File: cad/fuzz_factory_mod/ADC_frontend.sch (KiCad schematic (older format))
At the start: 11 parts

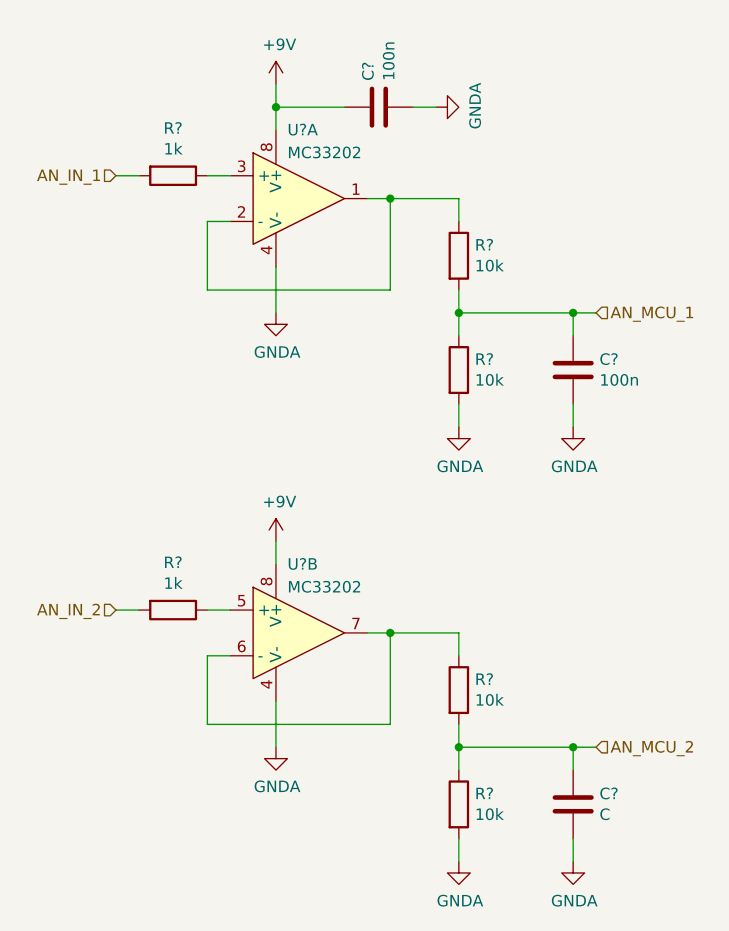
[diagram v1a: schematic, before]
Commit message: Continued schematic.
Modified fuuz_factory circuit : use of matched transistor pairs.
Added USB interface, through FT230X and direct to MCU.
Associated footprints, except for XTAL and trimmers.
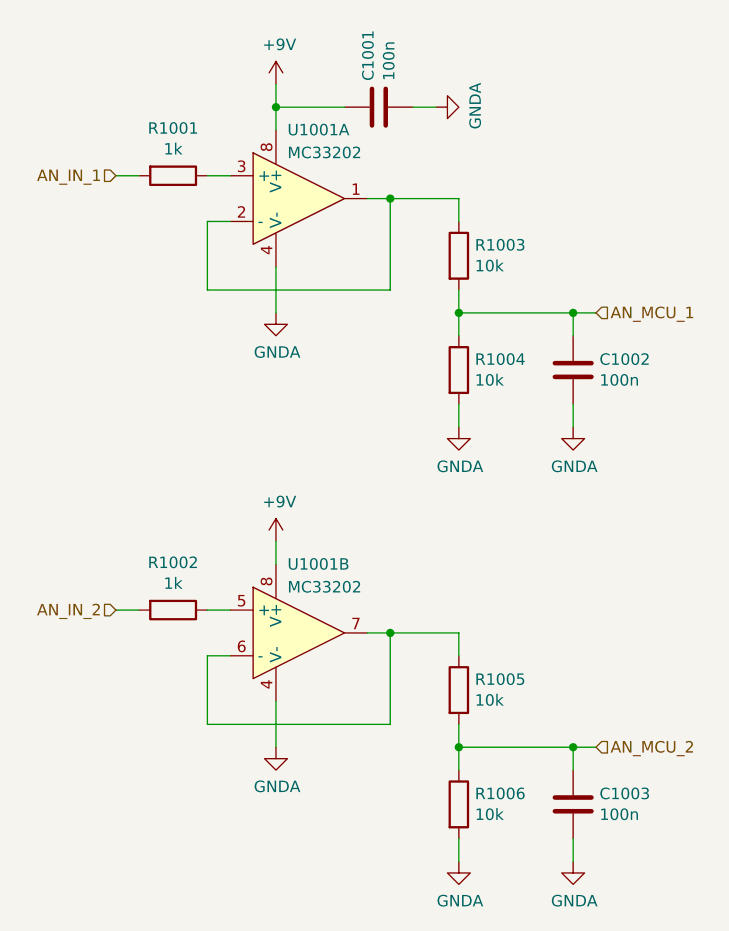
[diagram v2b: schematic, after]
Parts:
- C1001, C1002: renamed from C?; footprint (none) -> Capacitors_SMD:C_0603
- C1003: renamed from C?; value C -> 100n; footprint (none) -> Capacitors_SMD:C_0603
- R1001, R1002, R1003, R1004, R1005, R1006: renamed from R?; footprint (none) -> Resistors_SMD:R_0603
- U1001: renamed from U?; footprint (none) -> Housings_SOIC:SOIC-8_3.9x4.9mm_Pitch1.27mm
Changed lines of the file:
@@
 $Descr A4 11693 8268
 encoding utf-8
-Sheet 8 19
+Sheet 10 22
 Title ""
 Date ""
@@
 $EndDescr
 $Comp
-L power:+9V #PWR?
+L power:+9V #PWR01001
 U 1 1 5E671148
 P 2200 1600
-F 0 "#PWR?" H 2200 1450 50  0001 C CNN
+F 0 "#PWR01001" H 2200 1450 50  0001 C CNN
 F 1 "+9V" H 2215 1773 50  0000 C CNN
 F 2 "" H 2200 1600 50  0001 C CNN
@@
 $EndComp
 $Comp
-L power:GNDA #PWR?
+L power:GNDA #PWR01002
 U 1 1 5E672355
 P 2200 2600
-F 0 "#PWR?" H 2200 2350 50  0001 C CNN
+F 0 "#PWR01002" H 2200 2350 50  0001 C CNN
 F 1 "GNDA" H 2205 2427 50  0000 C CNN
 F 2 "" H 2200 2600 50  0001 C CNN
@@
 	2700 2100 2600 2100
 $Comp
-L flax_lib:MC33202 U?
+L flax_lib:MC33202 U1001
 U 1 1 5E66FC5B
 P 2300 2100
-F 0 "U?" H 2250 2400 50  0000 L CNN
+F 0 "U1001" H 2250 2400 50  0000 L CNN
 F 1 "MC33202" H 2250 2300 50  0000 L CNN
-F 2 "" H 2300 2100 50  0000 C CNN
+F 2 "Housings_SOIC:SOIC-8_3.9x4.9mm_Pitch1.27mm" H 2300 2100 50  0001 C CNN
 F 3 "" H 2250 1900 50  0000 L CNN
 	1    2300 2100
@@
 $EndComp
 $Comp
-L Device:R R?
+L Device:R R1003
 U 1 1 5E673C44
 P 3000 2350
-F 0 "R?" H 3070 2396 50  0000 L CNN
+F 0 "R1003" H 3070 2396 50  0000 L CNN
 F 1 "10k" H 3070 2305 50  0000 L CNN
-F 2 "" V 2930 2350 50  0001 C CNN
+F 2 "Resistors_SMD:R_0603" V 2930 2350 50  0001 C CNN
 F 3 "~" H 3000 2350 50  0001 C CNN
 	1    3000 2350
@@
 $EndComp
 $Comp
-L Device:R R?
+L Device:R R1004
 U 1 1 5E6750F5
 P 3000 2850
-F 0 "R?" H 3070 2896 50  0000 L CNN
+F 0 "R1004" H 3070 2896 50  0000 L CNN
 F 1 "10k" H 3070 2805 50  0000 L CNN
-F 2 "" V 2930 2850 50  0001 C CNN
+F 2 "Resistors_SMD:R_0603" V 2930 2850 50  0001 C CNN
 F 3 "~" H 3000 2850 50  0001 C CNN
 	1    3000 2850
@@
 $EndComp
 $Comp
-L power:GNDA #PWR?
+L power:GNDA #PWR01006
 U 1 1 5E6758D7
 P 3000 3100
-F 0 "#PWR?" H 3000 2850 50  0001 C CNN
+F 0 "#PWR01006" H 3000 2850 50  0001 C CNN
 F 1 "GNDA" H 3005 2927 50  0000 C CNN
 F 2 "" H 3000 3100 50  0001 C CNN
@@
 Connection ~ 2700 2100
 $Comp
-L Device:C C?
+L Device:C C1002
 U 1 1 5E676167
 P 3500 2850
-F 0 "C?" H 3615 2896 50  0000 L CNN
+F 0 "C1002" H 3615 2896 50  0000 L CNN
 F 1 "100n" H 3615 2805 50  0000 L CNN
-F 2 "" H 3538 2700 50  0001 C CNN
+F 2 "Capacitors_SMD:C_0603" H 3538 2700 50  0001 C CNN
 F 3 "~" H 3500 2850 50  0001 C CNN
 	1    3500 2850
@@
 	3000 2600 3000 2500
 $Comp
-L power:GNDA #PWR?
+L power:GNDA #PWR01008
 U 1 1 5E6770AE
 P 3500 3100
-F 0 "#PWR?" H 3500 2850 50  0001 C CNN
+F 0 "#PWR01008" H 3500 2850 50  0001 C CNN
 F 1 "GNDA" H 3505 2927 50  0000 C CNN
 F 2 "" H 3500 3100 50  0001 C CNN
@@
 	3500 3000 3500 3100
 $Comp
-L Device:R R?
+L Device:R R1001
 U 1 1 5E6776A2
 P 1750 2000
-F 0 "R?" V 1543 2000 50  0000 C CNN
+F 0 "R1001" V 1543 2000 50  0000 C CNN
 F 1 "1k" V 1634 2000 50  0000 C CNN
-F 2 "" V 1680 2000 50  0001 C CNN
+F 2 "Resistors_SMD:R_0603" V 1680 2000 50  0001 C CNN
 F 3 "~" H 1750 2000 50  0001 C CNN
 	1    1750 2000
@@
 Connection ~ 3500 2600
 $Comp
-L power:+9V #PWR?
+L power:+9V #PWR01003
 U 1 1 5E678DD1
 P 2200 3600
-F 0 "#PWR?" H 2200 3450 50  0001 C CNN
+F 0 "#PWR01003" H 2200 3450 50  0001 C CNN
 F 1 "+9V" H 2215 3773 50  0000 C CNN
 F 2 "" H 2200 3600 50  0001 C CNN
@@
 	2200 3600 2200 3700
 $Comp
-L power:GNDA #PWR?
+L power:GNDA #PWR01004
 U 1 1 5E678DDC
 P 2200 4500
-F 0 "#PWR?" H 2200 4250 50  0001 C CNN
+F 0 "#PWR01004" H 2200 4250 50  0001 C CNN
 F 1 "GNDA" H 2205 4327 50  0000 C CNN
 F 2 "" H 2200 4500 50  0001 C CNN
@@
 	2700 4000 2600 4000
 $Comp
-L flax_lib:MC33202 U?
+L flax_lib:MC33202 U1001
 U 2 1 5E678DEC
 P 2300 4000
-F 0 "U?" H 2250 4300 50  0000 L CNN
+F 0 "U1001" H 2250 4300 50  0000 L CNN
 F 1 "MC33202" H 2250 4200 50  0000 L CNN
-F 2 "" H 2300 4000 50  0000 C CNN
+F 2 "Housings_SOIC:SOIC-8_3.9x4.9mm_Pitch1.27mm" H 2300 4000 50  0001 C CNN
 F 3 "" H 2250 3800 50  0000 L CNN
 	2    2300 4000
@@
 $EndComp
 $Comp
-L Device:R R?
+L Device:R R1005
 U 1 1 5E678DF6
 P 3000 4250
-F 0 "R?" H 3070 4296 50  0000 L CNN
+F 0 "R1005" H 3070 4296 50  0000 L CNN
 F 1 "10k" H 3070 4205 50  0000 L CNN
-F 2 "" V 2930 4250 50  0001 C CNN
+F 2 "Resistors_SMD:R_0603" V 2930 4250 50  0001 C CNN
 F 3 "~" H 3000 4250 50  0001 C CNN
 	1    3000 4250
@@
 $EndComp
 $Comp
-L Device:R R?
+L Device:R R1006
 U 1 1 5E678E00
 P 3000 4750
-F 0 "R?" H 3070 4796 50  0000 L CNN
+F 0 "R1006" H 3070 4796 50  0000 L CNN
 F 1 "10k" H 3070 4705 50  0000 L CNN
-F 2 "" V 2930 4750 50  0001 C CNN
+F 2 "Resistors_SMD:R_0603" V 2930 4750 50  0001 C CNN
 F 3 "~" H 3000 4750 50  0001 C CNN
 	1    3000 4750
@@
 $EndComp
 $Comp
-L power:GNDA #PWR?
+L power:GNDA #PWR01007
 U 1 1 5E678E0A
 P 3000 5000
-F 0 "#PWR?" H 3000 4750 50  0001 C CNN
+F 0 "#PWR01007" H 3000 4750 50  0001 C CNN
 F 1 "GNDA" H 3005 4827 50  0000 C CNN
 F 2 "" H 3000 5000 50  0001 C CNN
@@
 Connection ~ 2700 4000
 $Comp
-L Device:C C?
+L Device:C C1003
 U 1 1 5E678E19
 P 3500 4750
-F 0 "C?" H 3615 4796 50  0000 L CNN
-F 1 "C" H 3615 4705 50  0000 L CNN
-F 2 "" H 3538 4600 50  0001 C CNN
+F 0 "C1003" H 3615 4796 50  0000 L CNN
+F 1 "100n" H 3615 4705 50  0000 L CNN
+F 2 "Capacitors_SMD:C_0603" H 3538 4600 50  0001 C CNN
 F 3 "~" H 3500 4750 50  0001 C CNN
 	1    3500 4750
@@
 	3000 4500 3000 4400
 $Comp
-L power:GNDA #PWR?
+L power:GNDA #PWR01009
 U 1 1 5E678E27
 P 3500 5000
-F 0 "#PWR?" H 3500 4750 50  0001 C CNN
+F 0 "#PWR01009" H 3500 4750 50  0001 C CNN
 F 1 "GNDA" H 3505 4827 50  0000 C CNN
 F 2 "" H 3500 5000 50  0001 C CNN
@@
 	3500 4900 3500 5000
 $Comp
-L Device:R R?
+L Device:R R1002
 U 1 1 5E678E32
 P 1750 3900
-F 0 "R?" V 1543 3900 50  0000 C CNN
+F 0 "R1002" V 1543 3900 50  0000 C CNN
 F 1 "1k" V 1634 3900 50  0000 C CNN
-F 2 "" V 1680 3900 50  0001 C CNN
+F 2 "Resistors_SMD:R_0603" V 1680 3900 50  0001 C CNN
 F 3 "~" H 1750 3900 50  0001 C CNN
 	1    1750 3900
@@
 Connection ~ 3500 4500
 $Comp
-L Device:C C?
+L Device:C C1001
 U 1 1 5E687CFA
 P 2650 1700
-F 0 "C?" H 2765 1746 50  0000 L CNN
+F 0 "C1001" H 2765 1746 50  0000 L CNN
 F 1 "100n" H 2765 1655 50  0000 L CNN
-F 2 "" H 2688 1550 50  0001 C CNN
+F 2 "Capacitors_SMD:C_0603" H 2688 1550 50  0001 C CNN
 F 3 "~" H 2650 1700 50  0001 C CNN
 	1    2650 1700
@@
 $EndComp
 $Comp
-L power:GNDA #PWR?
+L power:GNDA #PWR01005
 U 1 1 5E687D04
 P 2900 1700
-F 0 "#PWR?" H 2900 1450 50  0001 C CNN
+F 0 "#PWR01005" H 2900 1450 50  0001 C CNN
 F 1 "GNDA" H 2905 1527 50  0000 C CNN
 F 2 "" H 2900 1700 50  0001 C CNN

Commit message: Commit pre- board separation.
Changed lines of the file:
@@
 AR Path="/5DE4AD88/5E6E7BE0/5EEB4E87/5E671148" Ref="#PWR0119"  Part="1"
 AR Path="/5DE4AD88/5EB9A4D1/5ED2AE35/5E671148" Ref="#PWR02401"  Part="1"
-F 0 "#PWR0119" H 2200 1450 50  0001 C CNN
+F 0 "#PWR02401" H 2200 1450 50  0001 C CNN
 F 1 "+9V" H 2215 1773 50  0000 C CNN
 F 2 "" H 2200 1600 50  0001 C CNN
@@
 AR Path="/5DE4AD88/5E6E7BE0/5EEB4E87/5E672355" Ref="#PWR0120"  Part="1"
 AR Path="/5DE4AD88/5EB9A4D1/5ED2AE35/5E672355" Ref="#PWR02402"  Part="1"
-F 0 "#PWR0120" H 2200 2350 50  0001 C CNN
+F 0 "#PWR02402" H 2200 2350 50  0001 C CNN
 F 1 "GNDA" H 2205 2427 50  0000 C CNN
 F 2 "" H 2200 2600 50  0001 C CNN
@@
 AR Path="/5DE4AD88/5E6E7BE0/5EEB4E87/5E66FC5B" Ref="U1001"  Part="1"
 AR Path="/5DE4AD88/5EB9A4D1/5ED2AE35/5E66FC5B" Ref="U2401"  Part="1"
-F 0 "U1001" H 2250 2400 50  0000 L CNN
+F 0 "U2401" H 2250 2400 50  0000 L CNN
 F 1 "MC33202" H 2250 2300 50  0000 L CNN
 F 2 "Housings_SOIC:SOIC-8_3.9x4.9mm_Pitch1.27mm" H 2300 2100 50  0001 C CNN
@@
 AR Path="/5DE4AD88/5E6E7BE0/5EEB4E87/5E673C44" Ref="R1003"  Part="1"
 AR Path="/5DE4AD88/5EB9A4D1/5ED2AE35/5E673C44" Ref="R2403"  Part="1"
-F 0 "R1003" H 3070 2396 50  0000 L CNN
+F 0 "R2403" H 3070 2396 50  0000 L CNN
 F 1 "10k" H 3070 2305 50  0000 L CNN
 F 2 "Resistors_SMD:R_0603" V 2930 2350 50  0001 C CNN
@@
 AR Path="/5DE4AD88/5E6E7BE0/5EEB4E87/5E6750F5" Ref="R1004"  Part="1"
 AR Path="/5DE4AD88/5EB9A4D1/5ED2AE35/5E6750F5" Ref="R2404"  Part="1"
-F 0 "R1004" H 3070 2896 50  0000 L CNN
+F 0 "R2404" H 3070 2896 50  0000 L CNN
 F 1 "10k" H 3070 2805 50  0000 L CNN
 F 2 "Resistors_SMD:R_0603" V 2930 2850 50  0001 C CNN
@@
 AR Path="/5DE4AD88/5E6E7BE0/5EEB4E87/5E6758D7" Ref="#PWR0121"  Part="1"
 AR Path="/5DE4AD88/5EB9A4D1/5ED2AE35/5E6758D7" Ref="#PWR02406"  Part="1"
-F 0 "#PWR0121" H 3000 2850 50  0001 C CNN
+F 0 "#PWR02406" H 3000 2850 50  0001 C CNN
 F 1 "GNDA" H 3005 2927 50  0000 C CNN
 F 2 "" H 3000 3100 50  0001 C CNN
@@
 AR Path="/5DE4AD88/5E6E7BE0/5EEB4E87/5E676167" Ref="C1002"  Part="1"
 AR Path="/5DE4AD88/5EB9A4D1/5ED2AE35/5E676167" Ref="C2402"  Part="1"
-F 0 "C1002" H 3615 2896 50  0000 L CNN
+F 0 "C2402" H 3615 2896 50  0000 L CNN
 F 1 "100n" H 3615 2805 50  0000 L CNN
 F 2 "Capacitors_SMD:C_0603" H 3538 2700 50  0001 C CNN
@@
 AR Path="/5DE4AD88/5E6E7BE0/5EEB4E87/5E6770AE" Ref="#PWR0122"  Part="1"
 AR Path="/5DE4AD88/5EB9A4D1/5ED2AE35/5E6770AE" Ref="#PWR02408"  Part="1"
-F 0 "#PWR0122" H 3500 2850 50  0001 C CNN
+F 0 "#PWR02408" H 3500 2850 50  0001 C CNN
 F 1 "GNDA" H 3505 2927 50  0000 C CNN
 F 2 "" H 3500 3100 50  0001 C CNN
@@
 AR Path="/5DE4AD88/5E6E7BE0/5EEB4E87/5E6776A2" Ref="R1001"  Part="1"
 AR Path="/5DE4AD88/5EB9A4D1/5ED2AE35/5E6776A2" Ref="R2401"  Part="1"
-F 0 "R1001" V 1543 2000 50  0000 C CNN
+F 0 "R2401" V 1543 2000 50  0000 C CNN
 F 1 "1k" V 1634 2000 50  0000 C CNN
 F 2 "Resistors_SMD:R_0603" V 1680 2000 50  0001 C CNN
@@
 AR Path="/5DE4AD88/5E6E7BE0/5EEB4E87/5E678DD1" Ref="#PWR0123"  Part="1"
 AR Path="/5DE4AD88/5EB9A4D1/5ED2AE35/5E678DD1" Ref="#PWR02403"  Part="1"
-F 0 "#PWR0123" H 2200 3450 50  0001 C CNN
+F 0 "#PWR02403" H 2200 3450 50  0001 C CNN
 F 1 "+9V" H 2215 3773 50  0000 C CNN
 F 2 "" H 2200 3600 50  0001 C CNN
@@
 AR Path="/5DE4AD88/5E6E7BE0/5EEB4E87/5E678DDC" Ref="#PWR0124"  Part="1"
 AR Path="/5DE4AD88/5EB9A4D1/5ED2AE35/5E678DDC" Ref="#PWR02404"  Part="1"
-F 0 "#PWR0124" H 2200 4250 50  0001 C CNN
+F 0 "#PWR02404" H 2200 4250 50  0001 C CNN
 F 1 "GNDA" H 2205 4327 50  0000 C CNN
 F 2 "" H 2200 4500 50  0001 C CNN
@@
 AR Path="/5DE4AD88/5E6E7BE0/5EEB4E87/5E678DEC" Ref="U1001"  Part="2"
 AR Path="/5DE4AD88/5EB9A4D1/5ED2AE35/5E678DEC" Ref="U2401"  Part="2"
-F 0 "U1001" H 2250 4300 50  0000 L CNN
+F 0 "U2401" H 2250 4300 50  0000 L CNN
 F 1 "MC33202" H 2250 4200 50  0000 L CNN
 F 2 "Housings_SOIC:SOIC-8_3.9x4.9mm_Pitch1.27mm" H 2300 4000 50  0001 C CNN
@@
 AR Path="/5DE4AD88/5E6E7BE0/5EEB4E87/5E678DF6" Ref="R1005"  Part="1"
 AR Path="/5DE4AD88/5EB9A4D1/5ED2AE35/5E678DF6" Ref="R2405"  Part="1"
-F 0 "R1005" H 3070 4296 50  0000 L CNN
+F 0 "R2405" H 3070 4296 50  0000 L CNN
 F 1 "10k" H 3070 4205 50  0000 L CNN
 F 2 "Resistors_SMD:R_0603" V 2930 4250 50  0001 C CNN
@@
 AR Path="/5DE4AD88/5E6E7BE0/5EEB4E87/5E678E00" Ref="R1006"  Part="1"
 AR Path="/5DE4AD88/5EB9A4D1/5ED2AE35/5E678E00" Ref="R2406"  Part="1"
-F 0 "R1006" H 3070 4796 50  0000 L CNN
+F 0 "R2406" H 3070 4796 50  0000 L CNN
 F 1 "10k" H 3070 4705 50  0000 L CNN
 F 2 "Resistors_SMD:R_0603" V 2930 4750 50  0001 C CNN
@@
 AR Path="/5DE4AD88/5E6E7BE0/5EEB4E87/5E678E0A" Ref="#PWR0125"  Part="1"
 AR Path="/5DE4AD88/5EB9A4D1/5ED2AE35/5E678E0A" Ref="#PWR02407"  Part="1"
-F 0 "#PWR0125" H 3000 4750 50  0001 C CNN
+F 0 "#PWR02407" H 3000 4750 50  0001 C CNN
 F 1 "GNDA" H 3005 4827 50  0000 C CNN
 F 2 "" H 3000 5000 50  0001 C CNN
@@
 AR Path="/5DE4AD88/5E6E7BE0/5EEB4E87/5E678E19" Ref="C1003"  Part="1"
 AR Path="/5DE4AD88/5EB9A4D1/5ED2AE35/5E678E19" Ref="C2403"  Part="1"
-F 0 "C1003" H 3615 4796 50  0000 L CNN
+F 0 "C2403" H 3615 4796 50  0000 L CNN
 F 1 "100n" H 3615 4705 50  0000 L CNN
 F 2 "Capacitors_SMD:C_0603" H 3538 4600 50  0001 C CNN
@@
 AR Path="/5DE4AD88/5E6E7BE0/5EEB4E87/5E678E27" Ref="#PWR0126"  Part="1"
 AR Path="/5DE4AD88/5EB9A4D1/5ED2AE35/5E678E27" Ref="#PWR02409"  Part="1"
-F 0 "#PWR0126" H 3500 4750 50  0001 C CNN
+F 0 "#PWR02409" H 3500 4750 50  0001 C CNN
 F 1 "GNDA" H 3505 4827 50  0000 C CNN
 F 2 "" H 3500 5000 50  0001 C CNN
@@
 AR Path="/5DE4AD88/5E6E7BE0/5EEB4E87/5E678E32" Ref="R1002"  Part="1"
 AR Path="/5DE4AD88/5EB9A4D1/5ED2AE35/5E678E32" Ref="R2402"  Part="1"
-F 0 "R1002" V 1543 3900 50  0000 C CNN
+F 0 "R2402" V 1543 3900 50  0000 C CNN
 F 1 "1k" V 1634 3900 50  0000 C CNN
 F 2 "Resistors_SMD:R_0603" V 1680 3900 50  0001 C CNN
@@
 AR Path="/5DE4AD88/5E6E7BE0/5EEB4E87/5E687CFA" Ref="C1001"  Part="1"
 AR Path="/5DE4AD88/5EB9A4D1/5ED2AE35/5E687CFA" Ref="C2401"  Part="1"
-F 0 "C1001" H 2765 1746 50  0000 L CNN
+F 0 "C2401" H 2765 1746 50  0000 L CNN
 F 1 "100n" H 2765 1655 50  0000 L CNN
 F 2 "Capacitors_SMD:C_0603" H 2688 1550 50  0001 C CNN
@@
 AR Path="/5DE4AD88/5E6E7BE0/5EEB4E87/5E687D04" Ref="#PWR0127"  Part="1"
 AR Path="/5DE4AD88/5EB9A4D1/5ED2AE35/5E687D04" Ref="#PWR02405"  Part="1"
-F 0 "#PWR0127" H 2900 1450 50  0001 C CNN
+F 0 "#PWR02405" H 2900 1450 50  0001 C CNN
 F 1 "GNDA" H 2905 1527 50  0000 C CNN
 F 2 "" H 2900 1700 50  0001 C CNN
